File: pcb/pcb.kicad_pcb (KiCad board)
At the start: 2 copper layers, 61 x 118.2 mm, 10 parts, among them J1 Conn_01x32_Male, J2 Conn_01x32_Female, J3 Conn_01x06_Female, J4 Conn_01x05_Female, J5 Conn_02x14_Female, J6 Conn_02x16_Female

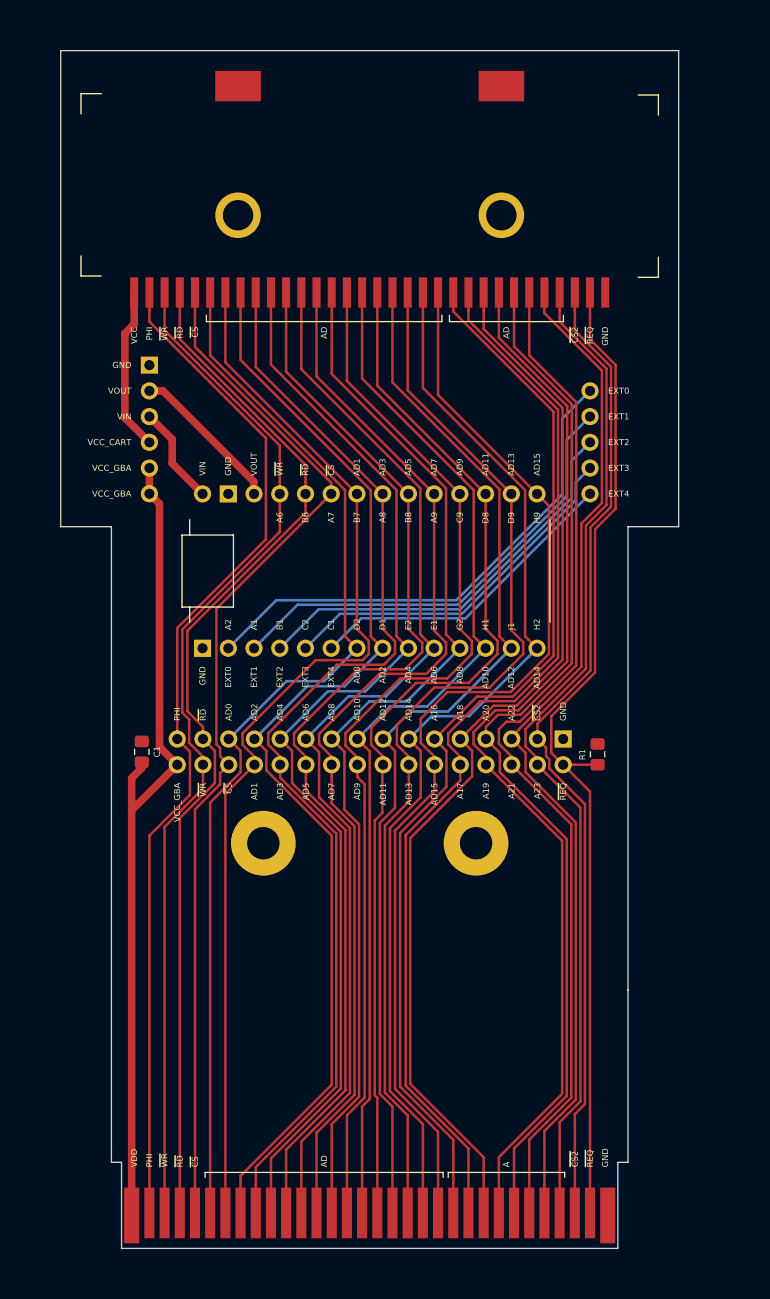
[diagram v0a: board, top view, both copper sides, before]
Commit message: Move headers to the other side
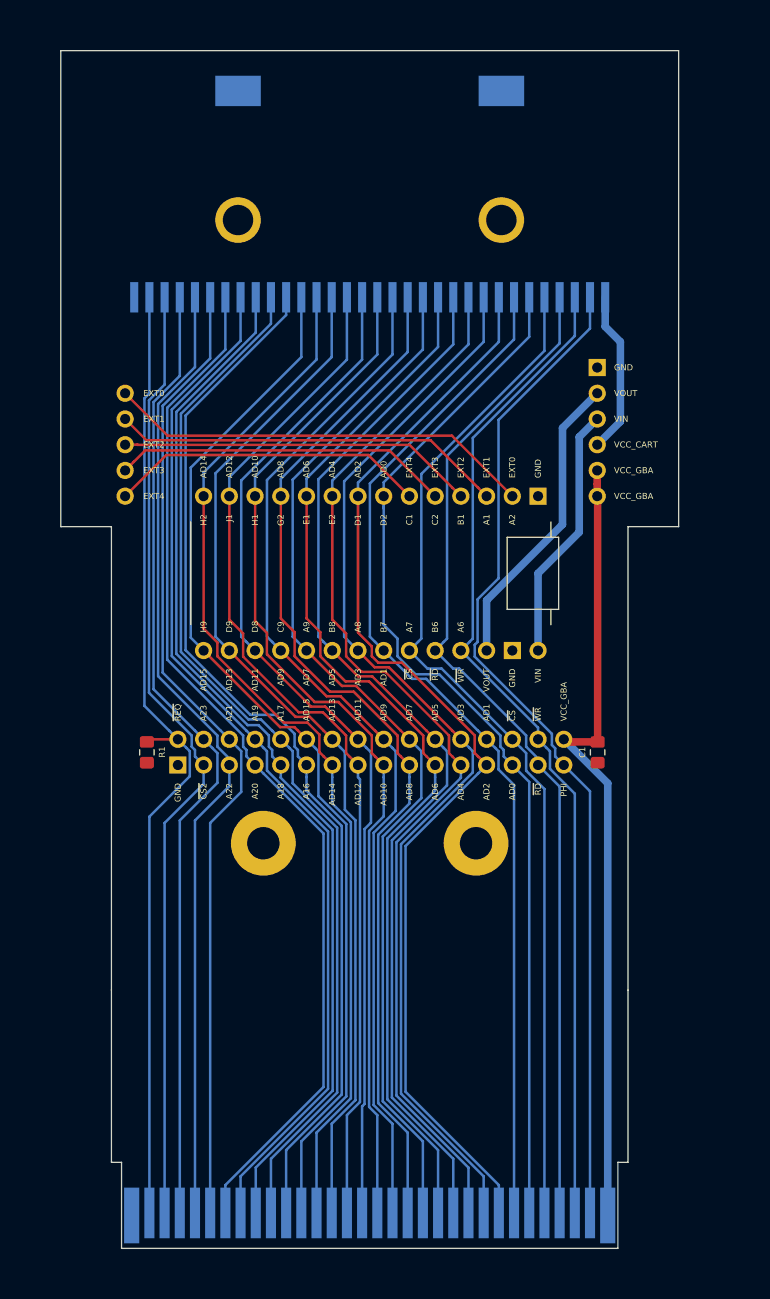
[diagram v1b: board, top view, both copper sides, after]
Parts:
- J1, J2: moved to B.Cu
- moved J2 49.0 mm to (87.0, 85.8), turned to 180 degrees
- moved J1 49.0 mm to (87.0, 176.5), turned to 180 degrees
- moved J4 45.9 mm to (38.4, 92.1)
- moved C1 45.0 mm to (85.0, 127.5), turned to 90 degrees
- moved R1 44.5 mm to (40.5, 127.5), turned to 90 degrees
- moved J3 44.2 mm to (85.0, 102.2)
- moved J6 38.2 mm to (81.7, 126.2), turned to 270 degrees
- moved J5 36.4 mm to (79.1, 102.2), turned to 270 degrees
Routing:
- net /VIN: track 9.80 -> 25.3 mm
- net /VOUT: track 15.2 -> 29.9 mm
- net /EXT0: track 50.6 -> 42.4 mm
- net /EXT1: track 45.9 -> 38.8 mm
- net /EXT2: track 41.2 -> 35.3 mm
- net /A21: track 101.4 -> 96.8 mm
- net /A22: track 100.8 -> 96.2 mm
- net /AD15: track 108.3 -> 103.9 mm
- net /AD13: track 106.4 -> 102.7 mm
- net /A23: track 99.2 -> 95.6 mm
- net /AD1: track 106.3 -> 103.0 mm
- net /EXT3: track 36.5 -> 33.3 mm
- net /AD11: track 104.9 -> 101.8 mm
- net /VCC_GBA: track 82.0 -> 79.1 mm
- net /~CS2: track 97.7 -> 94.9 mm
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
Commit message: Push latest version
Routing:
- net /AD1: track 103.0 -> 104.3 mm
- net /PHI: track 99.8 -> 100.6 mm
- net GND: vias 0 -> 6
- added copper zone on B.Cu, net GND
- added copper zone on F.Cu, net GND
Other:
- rule via_min_size: 0.4 -> 0.508
